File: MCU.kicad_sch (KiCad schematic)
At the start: 13 parts, among them J1 USB_C_Receptacle, SW3 SW_Push, SW4 SW_Push, SW5 SW_Push, SW6 SW_Push, U7 LSF0204GU12X, U8 FAN5622SX, U9 NORA-B106-00B, X608 Display

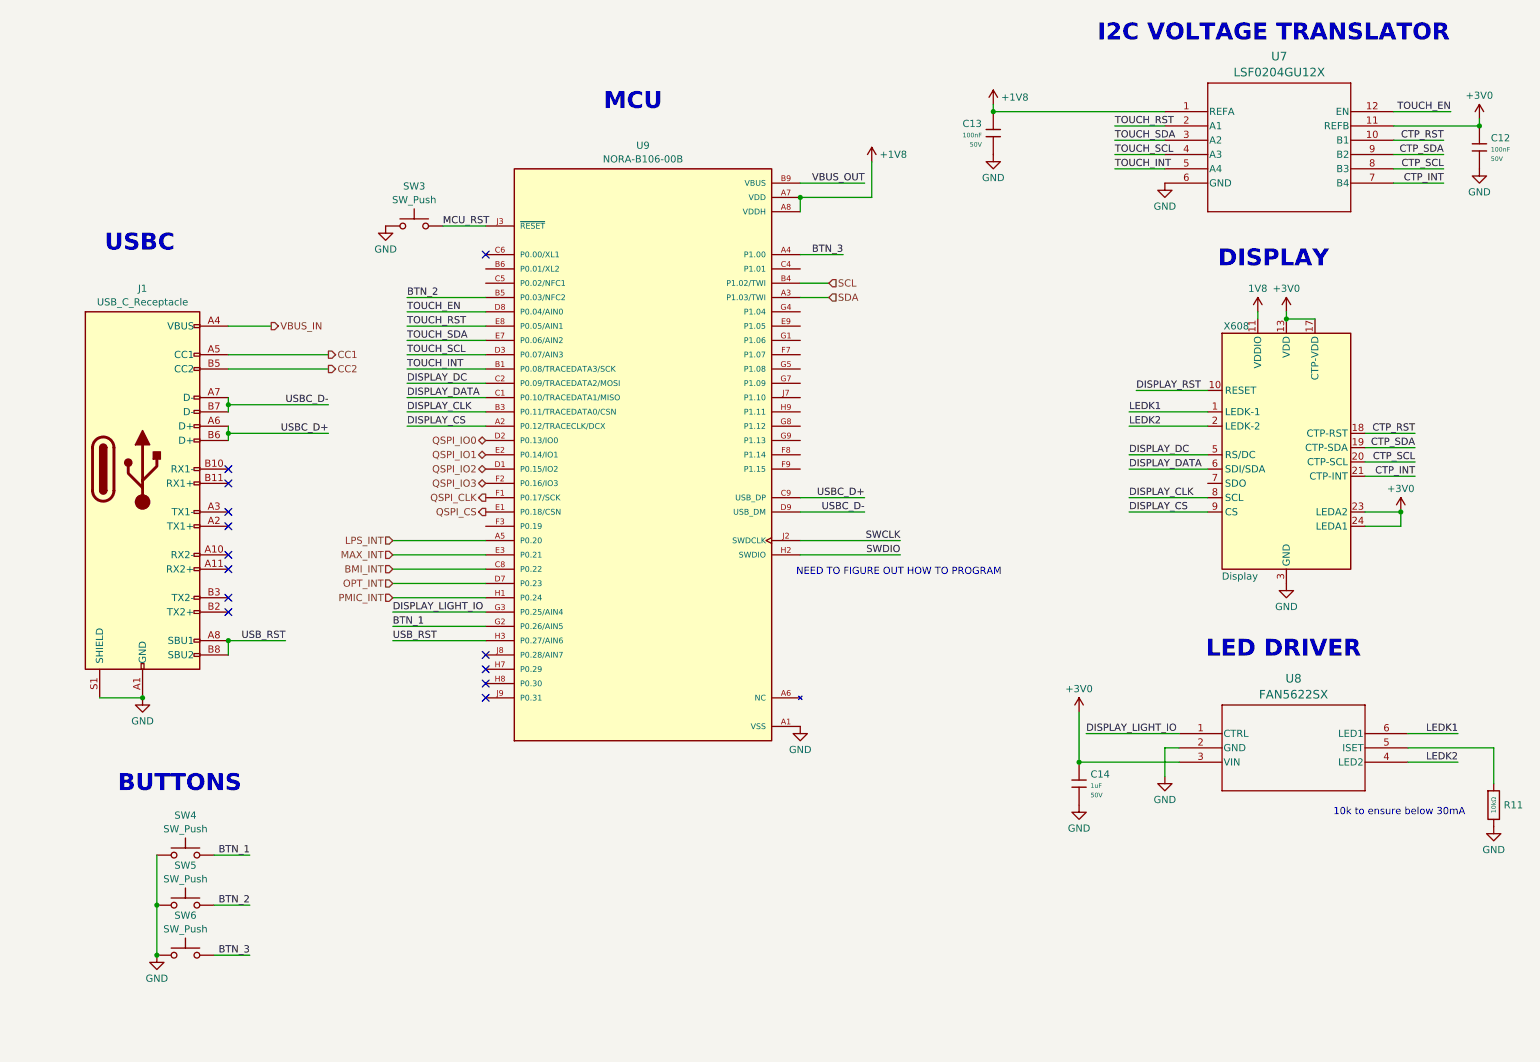
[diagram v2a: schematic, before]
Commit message: Added Vibration Motor & Prog Pinout
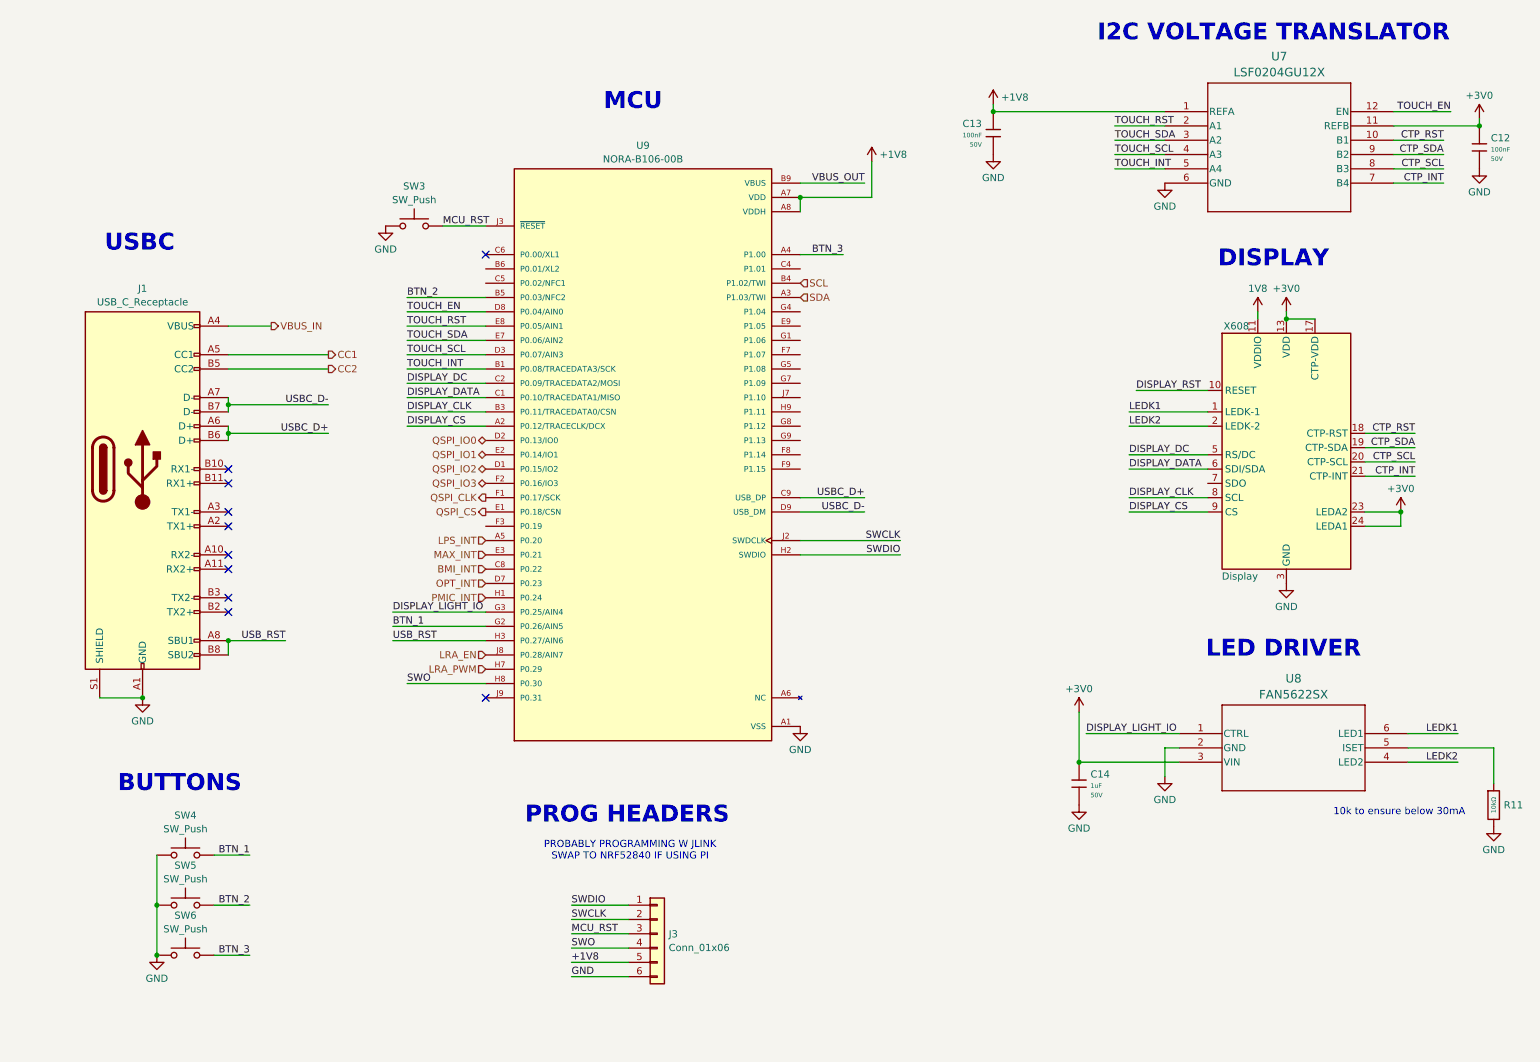
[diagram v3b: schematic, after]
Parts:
- added J3: Conn_01x06, symbol Connector_Generic:Conn_01x06
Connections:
- net +1V8: now also J3.5 (Pin_5)
- net GND: now also J3.6 (Pin_6)
- net MCU_RST: now also J3.3 (Pin_3)
- net SWCLK: now also J3.2 (Pin_2)
- net SWDIO: now also J3.1 (Pin_1)
- net LRA_PWM: now reaches U9.H7 (P0.29)
- net SWO: now reaches U9.H8 (P0.30)
- net SWO: now also J3.4 (Pin_4)
- net LRA_EN: now reaches U9.J8 (P0.28/AIN7)
- no-connect marks 13 -> 10
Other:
- note added: "PROBABLY PROGRAMMING W JLINK SWAP TO NRF52840 IF USING PI"
- note added: "PROG HEADERS"
- note removed: "NEED TO FIGURE OUT HOW TO PROGRAM"
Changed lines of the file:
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@@
-		)
-	)
-	(text "NEED TO FIGURE OUT HOW TO PROGRAM"
-		(exclude_from_sim no)
-		(at 172.466 112.268 0)
-		(effects
-			(font
-				(size 1.27 1.27)
-			)
 		)
 	)
@@
 		(exclude_from_sim no)
 		(at 125.222 28.702 0)
+		(effects
+			(font
+				(size 3 3)
+				(thickness 0.6)
+				(bold yes)
+			)
+		)
+	)
+	(text "PROBABLY PROGRAMMING W JLINK\nSWAP TO NRF52840 IF USING PI"
+		(exclude_from_sim no)
+		(at 124.714 161.798 0)
+		(effects
+			(font
+				(size 1.27 1.27)
+			)
+		)
+	)
+	(text "PROG HEADERS"
+		(exclude_from_sim no)
+		(at 124.206 155.448 0)
 		(effects
 			(font
@@
 	)
 	(no_connect
-		(at 99.06 132.08)
-	)
-	(no_connect
 		(at 53.34 104.14)
 	)
@@
 	)
 	(no_connect
-		(at 99.06 127)
-	)
-	(no_connect
 		(at 53.34 101.6)
 	)
@@
 	)
 	(no_connect
-		(at 99.06 129.54)
-	)
-	(no_connect
 		(at 53.34 119.38)
 	)
@@
 	(wire
 		(pts
-			(xy 160.02 63.5) (xy 154.94 63.5)
-		)
-		(stroke
-			(width 0)
-			(type default)
-		)
-	)
-	(wire
-		(pts
 			(xy 210.82 33.02) (xy 219.71 33.02)
 		)
@@
 	(wire
 		(pts
-			(xy 82.55 109.22) (xy 99.06 109.22)
+			(xy 114.3 173.99) (xy 124.46 173.99)
 		)
 		(stroke
@@
 	(wire
 		(pts
+			(xy 114.3 181.61) (xy 124.46 181.61)
+		)
+		(stroke
+			(width 0)
+			(type default)
+		)
+	)
+	(wire
+		(pts
 			(xy 222.25 143.51) (xy 219.71 143.51)
 		)
@@
 	(wire
 		(pts
+			(xy 114.3 176.53) (xy 124.46 176.53)
+		)
+		(stroke
+			(width 0)
+			(type default)
+		)
+	)
+	(wire
+		(pts
 			(xy 85.09 76.2) (xy 99.06 76.2)
 		)
@@
 	(wire
 		(pts
-			(xy 99.06 116.84) (xy 82.55 116.84)
-		)
-		(stroke
-			(width 0)
-			(type default)
-		)
-	)
-	(wire
-		(pts
 			(xy 278.13 143.51) (xy 278.13 149.86)
 		)
@@
 	(wire
 		(pts
+			(xy 114.3 179.07) (xy 124.46 179.07)
+		)
+		(stroke
+			(width 0)
+			(type default)
+		)
+	)
+	(wire
+		(pts
 			(xy 213.36 99.06) (xy 227.33 99.06)
 		)
@@
 	(wire
 		(pts
-			(xy 82.55 111.76) (xy 99.06 111.76)
-		)
-		(stroke
-			(width 0)
-			(type default)
-		)
-	)
-	(wire
-		(pts
 			(xy 260.35 30.48) (xy 270.51 30.48)
 		)
@@
 	(wire
 		(pts
+			(xy 114.3 171.45) (xy 124.46 171.45)
+		)
+		(stroke
+			(width 0)
+			(type default)
+		)
+	)
+	(wire
+		(pts
 			(xy 154.94 101.6) (xy 166.37 101.6)
 		)
@@
 	(wire
 		(pts
-			(xy 82.55 106.68) (xy 99.06 106.68)
-		)
-		(stroke
-			(width 0)
-			(type default)
-		)
-	)
-	(wire
-		(pts
 			(xy 204.47 137.16) (xy 204.47 146.05)
 		)
@@
 	(wire
 		(pts
-			(xy 82.55 114.3) (xy 99.06 114.3)
-		)
-		(stroke
-			(width 0)
-			(type default)
-		)
-	)
-	(wire
-		(pts
-			(xy 160.02 60.96) (xy 154.94 60.96)
-		)
-		(stroke
-			(width 0)
-			(type default)
-		)
-	)
-	(wire
-		(pts
 			(xy 85.09 63.5) (xy 99.06 63.5)
 		)
@@
 	(wire
 		(pts
+			(xy 114.3 184.15) (xy 124.46 184.15)
+		)
+		(stroke
+			(width 0)
+			(type default)
+		)
+	)
+	(wire
+		(pts
 			(xy 53.34 86.36) (xy 53.34 87.63)
 		)
@@
 		(pts
 			(xy 53.34 81.28) (xy 53.34 82.55)
+		)
+		(stroke
+			(width 0)
+			(type default)
+		)
+	)
+	(wire
+		(pts
+			(xy 85.09 132.08) (xy 99.06 132.08)
 		)
 		(stroke
@@
 		)
 	)
+	(label "SWO"
+		(at 85.09 132.08 0)
+		(effects
+			(font
+				(size 1.27 1.27)
+			)
+			(justify left bottom)
+		)
+	)
+	(label "SWO"
+		(at 114.3 179.07 0)
+		(effects
+			(font
+				(size 1.27 1.27)
+			)
+			(justify left bottom)
+		)
+	)
 	(label "CTP_SDA"
 		(at 264.16 90.17 180)
@@
 		)
 	)
+	(label "SWCLK"
+		(at 114.3 173.99 0)
+		(effects
+			(font
+				(size 1.27 1.27)
+			)
+			(justify left bottom)
+		)
+	)
 	(label "DISPLAY_RST"
 		(at 214.63 80.01 0)
@@
 		)
 	)
+	(label "MCU_RST"
+		(at 114.3 176.53 0)
+		(effects
+			(font
+				(size 1.27 1.27)
+			)
+			(justify left bottom)
+		)
+	)
 	(label "TOUCH_RST"
 		(at 85.09 68.58 0)
@@
 		)
 	)
+	(label "GND"
+		(at 114.3 184.15 0)
+		(effects
+			(font
+				(size 1.27 1.27)
+			)
+			(justify left bottom)
+		)
+	)
 	(label "DISPLAY_DC"
 		(at 213.36 91.44 0)
@@
 		)
 	)
+	(label "SWDIO"
+		(at 114.3 171.45 0)
+		(effects
+			(font
+				(size 1.27 1.27)
+			)
+			(justify left bottom)
+		)
+	)
 	(label "LEDK1"
 		(at 271.78 140.97 180)
@@
 		)
 	)
+	(label "+1V8"
+		(at 114.3 181.61 0)
+		(effects
+			(font
+				(size 1.27 1.27)
+			)
+			(justify left bottom)
+		)
+	)
 	(label "BTN_2"
 		(at 57.15 171.45 180)
@@
 	(hierarchical_label "SCL"
 		(shape input)
-		(at 160.02 60.96 0)
+		(at 154.94 60.96 0)
 		(effects
 			(font
@@
 	(hierarchical_label "LPS_INT"
 		(shape input)
-		(at 82.55 106.68 180)
+		(at 99.06 106.68 180)
 		(effects
 			(font
@@
 		)
 	)
+	(hierarchical_label "LRA_EN"
+		(shape input)
+		(at 99.06 127 180)
+		(effects
+			(font
+				(size 1.27 1.27)
+			)
+			(justify right)
+		)
+	)
 	(hierarchical_label "QSPI_IO2"
 		(shape bidirectional)
@@
 	(hierarchical_label "PMIC_INT"
 		(shape input)
-		(at 82.55 116.84 180)
+		(at 99.06 116.84 180)
 		(effects
 			(font
@@
 		)
 	)
+	(hierarchical_label "LRA_PWM"
+		(shape input)
+		(at 99.06 129.54 180)
+		(effects
+			(font
+				(size 1.27 1.27)
+			)
+			(justify right)
+		)
+	)
 	(hierarchical_label "SDA"
 		(shape input)
-		(at 160.02 63.5 0)
+		(at 154.94 63.5 0)
 		(effects
 			(font
@@
 	(hierarchical_label "OPT_INT"
 		(shape input)
-		(at 82.55 114.3 180)
+		(at 99.06 114.3 180)
 		(effects
 			(font
@@
 	(hierarchical_label "BMI_INT"
 		(shape input)
-		(at 82.55 111.76 180)
+		(at 99.06 111.76 180)
 		(effects
 			(font
@@
 	(hierarchical_label "MAX_INT"
 		(shape input)
-		(at 82.55 109.22 180)
+		(at 99.06 109.22 180)
 		(effects
 			(font
@@
 					(unit 1)
 				)
+			)
+		)
+	)
+	(symbol
+		(lib_id "Connector_Generic:Conn_01x06")
+		(at 129.54 176.53 0)
+		(unit 1)
+		(exclude_from_sim no)
+		(in_bom yes)
+		(on_board yes)
+		(dnp no)
+		(fields_autoplaced yes)
+		(property "Reference" "J3"
+			(at 131.572 176.5878 0)
+			(effects
+				(font
+					(size 1.27 1.27)
+				)
+				(justify left)
+			)
+		)
+		(property "Value" "Conn_01x06"
+			(at 131.572 179.0121 0)
+			(effects
+				(font
+					(size 1.27 1.27)
+				)
+				(justify left)
+			)
+		)
+		(property "Footprint" ""
+			(at 129.54 176.53 0)
+			(effects
+				(font
+					(size 1.27 1.27)
+				)
+				(hide yes)
+			)
+		)
+		(property "Datasheet" "~"
+			(at 129.54 176.53 0)
+			(effects
+				(font
+					(size 1.27 1.27)
+				)
+				(hide yes)
+			)
+		)
+		(property "Description" "Generic connector, single row, 01x06, script generated (kicad-library-utils/schlib/autogen/connector/)"
+			(at 129.54 176.53 0)
+			(effects
+				(font
+					(size 1.27 1.27)
+				)
+				(hide yes)
+			)
+		)
+		(pin "2"
+		)
+		(pin "6"
+		)
+		(pin "1"
+		)
+		(pin "4"
+		)
+		(pin "3"
+		)
+		(pin "5"
+		)
+		(instances
+			(project ""
+				(path "/69095a4d-0a57-4fa3-aecb-1cfd89eedc11/bed567dd-6d09-419a-b99a-3e57c9439bd4/30bd5bb3-3a33-4afa-baf2-7512abedf580"
+					(reference "J3")
+					(unit 1)
+				)

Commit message: Added clock and updated schem
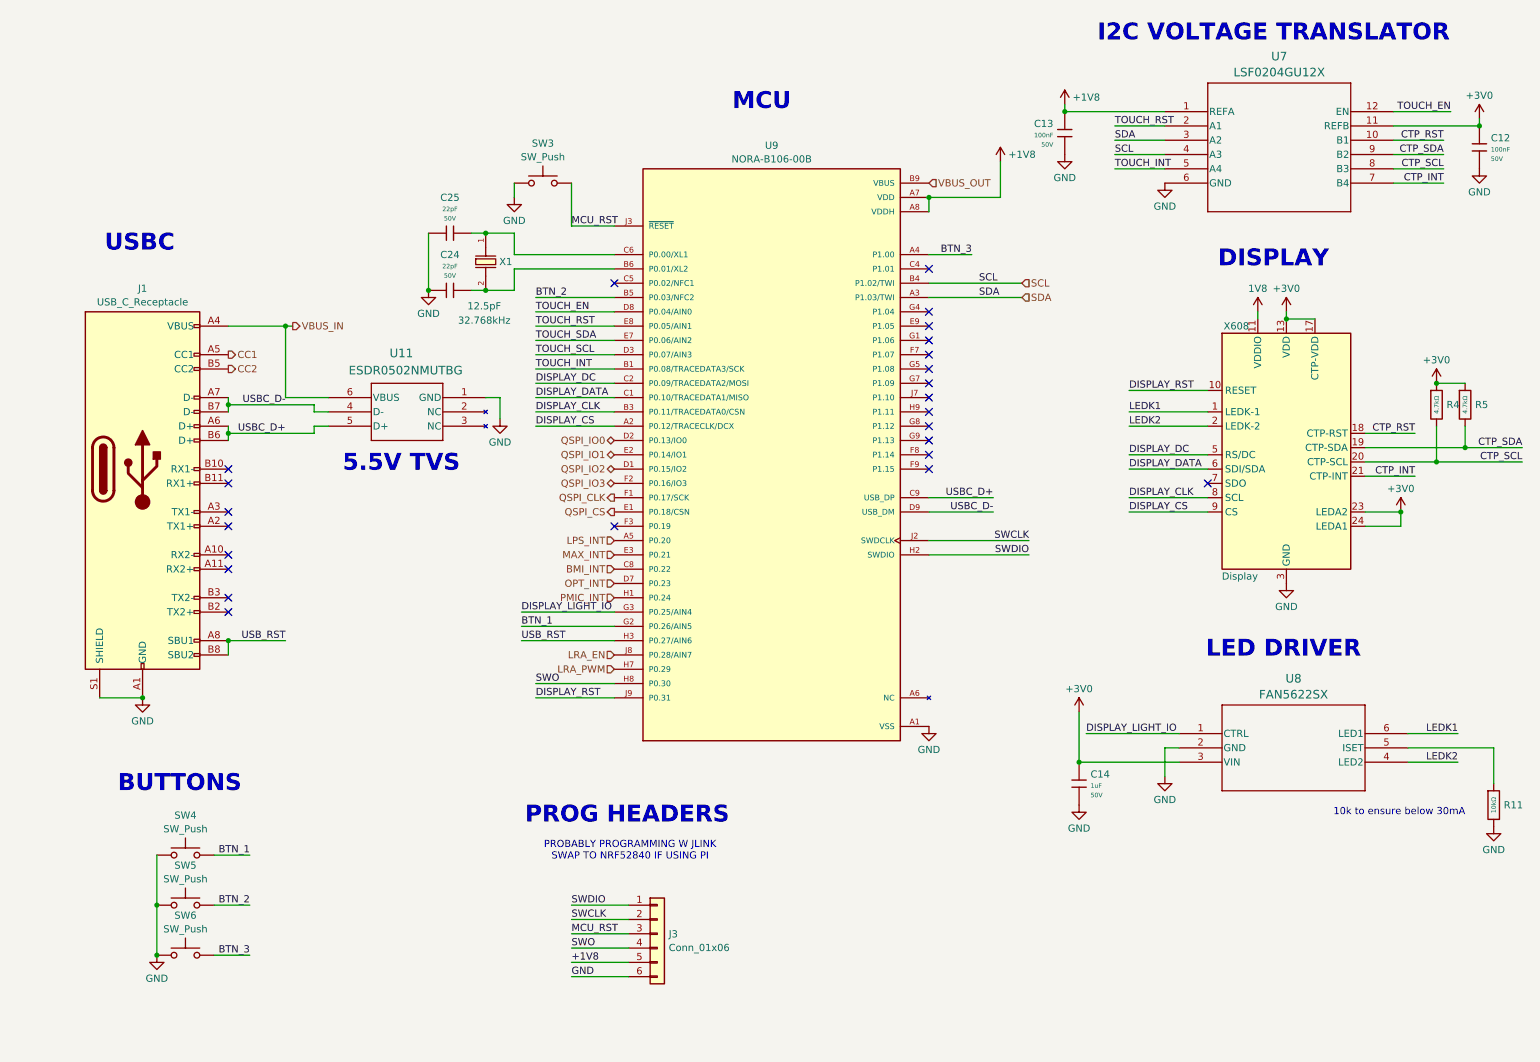
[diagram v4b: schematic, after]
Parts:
- added C24, C25: 22pF, PCM_JLCPCB:C_0603, symbol PCM_JLCPCB-Capacitors:0603,22pF
- added R4, R5: 4.7kΩ, PCM_JLCPCB:R_0603, symbol PCM_JLCPCB-Resistors:0603,4.7kΩ
- added U11: ESDR0502NMUTBG, UDFN6_517AA_ONS, symbol 2026-04-16_01-33-00:ESDR0502NMUTBG
- added X1: Q13FC1350000400, PCM_JLCPCB:FC-135R_L3.2-W1.5, symbol PCM_JLCPCB-Crystals:Crystal, 32.768kHz, 13pF
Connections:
- net +3V0: now also R4.1, R5.1
- net CTP_SCL: now also R4.2
- net CTP_SDA: now also R5.2
- net DISPLAY_RST: now also U9.J9 (P0.31)
- net GND: now also C24.1, C25.1, U11.1 (GND)
- net SCL: now also U7.4 (A3)
- net SDA: now also U7.3 (A2)
- net TOUCH_SCL: no longer U7.4 (A3)
- net TOUCH_SDA: no longer U7.3 (A2)
- net USBC_D+: now also U11.5 (D+)
- net USBC_D-: now also U11.4 (D-)
- net VBUS_IN: now also U11.6 (VBUS)
- net at U9.B6 (P0.01/XL2): now also C24.2, X1.2
- net at U9.C6 (P0.00/XL1): now also C25.2, X1.1
- no-connect marks 10 -> 24
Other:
- note added: "5.5V TVS"
- moved on the sheet: C13, SW3, U9
